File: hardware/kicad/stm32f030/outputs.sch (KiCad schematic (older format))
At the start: 26 parts, among them K1 RELAY_1RT, K2 RELAY_1RT, P4 RELAY OUT 1, P5 TTL OUT 1, P6 RELAY OUT 2, P7 TTL OUT 2, Q5 BC817-40, Q6 BC817-40, Q7 BC817-40, Q8 BC817-40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

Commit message: hardware/kicad/stm32f030: modules ready
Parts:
- K1, K2: footprint Relays_THT:Relay_SANYOU_SRD_Series_Form_C -> relays:SRD-SL-C
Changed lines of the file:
@@
 F 0 "K1" H 3400 2050 50  0000 C CNN
 F 1 "RELAY_1RT" H 3550 1400 50  0000 C CNN
-F 2 "Relays_THT:Relay_SANYOU_SRD_Series_Form_C" H 3350 1900 50  0001 C CNN
+F 2 "relays:SRD-SL-C" H 3350 1900 50  0001 C CNN
 F 3 "" H 3350 1900 50  0000 C CNN
 	1    3400 1900
@@
 F 0 "K2" H 3400 4700 50  0000 C CNN
 F 1 "RELAY_1RT" H 3550 4050 50  0000 C CNN
-F 2 "Relays_THT:Relay_SANYOU_SRD_Series_Form_C" H 3350 4550 50  0001 C CNN
+F 2 "relays:SRD-SL-C" H 3350 4550 50  0001 C CNN
 F 3 "" H 3350 4550 50  0000 C CNN
 	1    3400 4550

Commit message: hardware/kicad/stm32f030: adding eeprom step2
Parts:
- K1, K2: footprint relays:SRD-SL-C -> cardetector:SRD-SL-C
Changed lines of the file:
@@
 F 0 "K1" H 3400 2050 50  0000 C CNN
 F 1 "RELAY_1RT" H 3550 1400 50  0000 C CNN
-F 2 "relays:SRD-SL-C" H 3350 1900 50  0001 C CNN
+F 2 "cardetector:SRD-SL-C" H 3350 1900 50  0001 C CNN
 F 3 "" H 3350 1900 50  0000 C CNN
 	1    3400 1900
@@
 F 0 "K2" H 3400 4700 50  0000 C CNN
 F 1 "RELAY_1RT" H 3550 4050 50  0000 C CNN
-F 2 "relays:SRD-SL-C" H 3350 4550 50  0001 C CNN
+F 2 "cardetector:SRD-SL-C" H 3350 4550 50  0001 C CNN
 F 3 "" H 3350 4550 50  0000 C CNN
 	1    3400 4550

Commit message: hardware/kicad/stm32f030: final touches
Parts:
- D1, D2: footprint Diodes_SMD:MELF_Standard -> Diodes_SMD:D_MiniMELF_Standard
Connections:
- net at K1.3 (R1): now also P4.3 (P3); no longer P4.1 (P1)
- net at K1.4 (T1): now also P4.1 (P1); no longer P4.3 (P3)
- net at K2.3 (R1): now also P6.3 (P3); no longer P6.1 (P1)
- net at K2.4 (T1): now also P6.1 (P1); no longer P6.3 (P3)
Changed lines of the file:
@@
 F 3 "" H 3150 1450 50  0000 C CNN
 	1    3150 1450
-	0    1    -1   0
+	0    -1   -1   0
 $EndComp
 $Comp
@@
 F 3 "" H 3150 4100 50  0000 C CNN
 	1    3150 4100
-	0    1    -1   0
+	0    -1   -1   0
 $EndComp
 $Comp
@@
 F 0 "D2" H 3850 4930 50  0000 L CNN
 F 1 "D_Small" H 3750 4770 50  0000 L CNN
-F 2 "Diodes_SMD:MELF_Standard" V 3900 4850 50  0001 C CNN
+F 2 "Diodes_SMD:D_MiniMELF_Standard" V 3900 4850 50  0001 C CNN
 F 3 "" V 3900 4850 50  0000 C CNN
 	1    3900 4850
@@
 F 0 "D1" H 3850 2280 50  0000 L CNN
 F 1 "D_Small" H 3750 2120 50  0000 L CNN
-F 2 "Diodes_SMD:MELF_Standard" V 3900 2200 50  0001 C CNN
+F 2 "Diodes_SMD:D_MiniMELF_Standard" V 3900 2200 50  0001 C CNN
 F 3 "" V 3900 2200 50  0000 C CNN
 	1    3900 2200

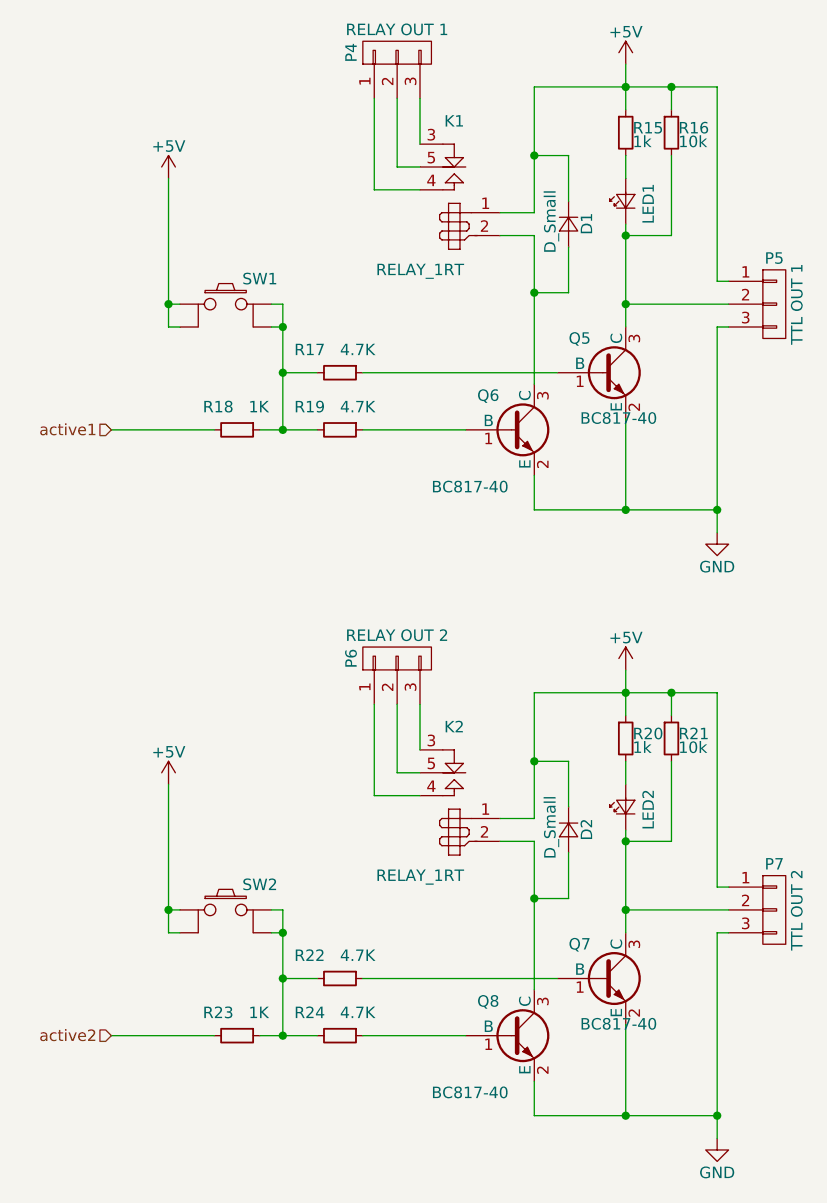
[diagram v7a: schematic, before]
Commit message: hardware/kicad/stm32f030: everything is connected, DRC OK
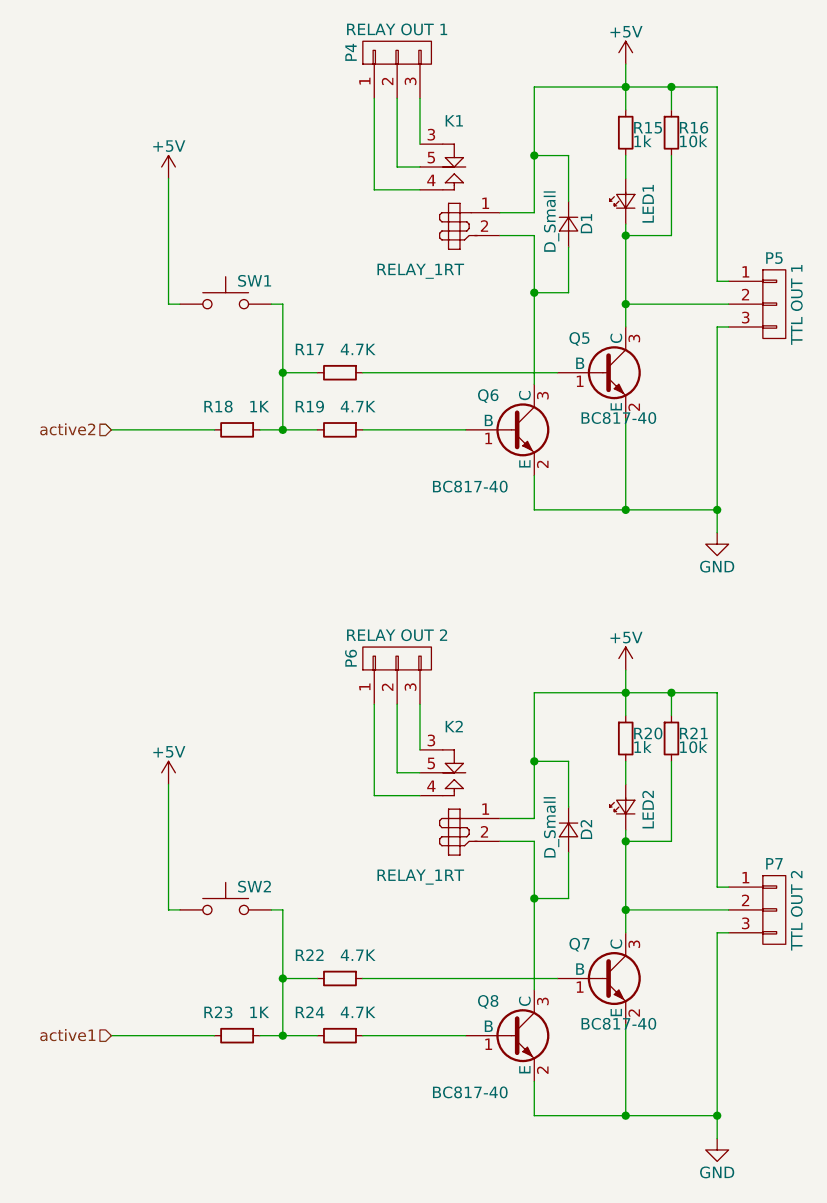
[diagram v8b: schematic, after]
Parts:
- removed SW1, SW2: TACTILE_SW, Buttons_Switches_THT:SW_PUSH_6mm, symbol TACTILE_SW
- added SW1, SW2: SW_Push, cardetector:TS_362, symbol SW_Push
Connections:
- net +5V: now also SW1.1, SW2.1
- net active1: now also R23.2; no longer R18.2
- net active2: now also R18.2; no longer R23.2
- net at R17.2, R18.1, R19.2: now also SW1.2
- net at R22.2, R23.1, R24.2: now also SW2.2
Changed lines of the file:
@@
 LIBS:transformer
 LIBS:stm32
+LIBS:switches
 LIBS:stm32f030-cache
 EELAYER 25 0
@@
 	0    -1   -1   0
 $EndComp
-$Comp
-L TACTILE_SW SW1
-U 1 1 575F7842
-P 2400 2550
-F 0 "SW1" H 2550 2660 50  0000 C CNN
-F 1 "TACTILE_SW" H 2420 2410 50  0001 C CNN
-F 2 "Buttons_Switches_THT:SW_PUSH_6mm" H 2400 2550 50  0001 C CNN
-F 3 "" H 2400 2550 50  0000 C CNN
-	1    2400 2550
-	1    0    0    -1
-$EndComp
 Wire Wire Line
 	2550 3100 2800 3100
@@
 	2600 2550 2650 2550
 Connection ~ 2650 2850
-Wire Wire Line
-	2600 2650 2650 2650
-Connection ~ 2650 2650
-Wire Wire Line
-	2150 2650 2200 2650
-Wire Wire Line
-	2150 2000 2150 2650
-Wire Wire Line
-	2150 2550 2200 2550
 $Comp
 L +5V #PWR028
@@
 	1    0    0    -1
 $EndComp
-Connection ~ 2150 2550
 $Comp
 L R_Small R16
@@
 Connection ~ 4550 3450
 Connection ~ 4150 3450
-Text HLabel 1900 3100 0    50   Input ~ 0
+Text HLabel 1900 5750 0    50   Input ~ 0
 active1
 $Comp
@@
 	0    -1   -1   0
 $EndComp
-$Comp
-L TACTILE_SW SW2
-U 1 1 5884C4BD
-P 2400 5200
-F 0 "SW2" H 2550 5310 50  0000 C CNN
-F 1 "TACTILE_SW" H 2420 5060 50  0001 C CNN
-F 2 "Buttons_Switches_THT:SW_PUSH_6mm" H 2400 5200 50  0001 C CNN
-F 3 "" H 2400 5200 50  0000 C CNN
-	1    2400 5200
-	1    0    0    -1
-$EndComp
 Wire Wire Line
 	2550 5750 2800 5750
@@
 	2600 5200 2650 5200
 Connection ~ 2650 5500
-Wire Wire Line
-	2600 5300 2650 5300
-Connection ~ 2650 5300
-Wire Wire Line
-	2150 5300 2200 5300
-Wire Wire Line
-	2150 4650 2150 5300
-Wire Wire Line
-	2150 5200 2200 5200
 $Comp
 L +5V #PWR031
@@
 	1    0    0    -1
 $EndComp
-Connection ~ 2150 5200
 $Comp
 L R_Small R21
@@
 Connection ~ 4550 6100
 Connection ~ 4150 6100
-Text HLabel 1900 5750 0    50   Input ~ 0
+Text HLabel 1900 3100 0    50   Input ~ 0
 active2
 $Comp
@@
 	3900 2500 3750 2500
 Connection ~ 3750 2500
+$Comp
+L SW_Push SW1
+U 1 1 58B3F079
+P 2400 2550
+F 0 "SW1" H 2450 2650 50  0000 L CNN
+F 1 "SW_Push" H 2400 2490 50  0001 C CNN
+F 2 "cardetector:TS_362" H 2400 2750 50  0001 C CNN
+F 3 "" H 2400 2750 50  0000 C CNN
+	1    2400 2550
+	1    0    0    -1
+$EndComp
+Wire Wire Line
+	2200 2550 2150 2550
+Wire Wire Line
+	2150 2550 2150 2000
+$Comp
+L SW_Push SW2
+U 1 1 58B3F67F
+P 2400 5200
+F 0 "SW2" H 2450 5300 50  0000 L CNN
+F 1 "SW_Push" H 2400 5140 50  0001 C CNN
+F 2 "cardetector:TS_362" H 2400 5400 50  0001 C CNN
+F 3 "" H 2400 5400 50  0000 C CNN
+	1    2400 5200
+	1    0    0    -1
+$EndComp
+Wire Wire Line
+	2200 5200 2150 5200
+Wire Wire Line
+	2150 5200 2150 4650
 $EndSCHEMATC
